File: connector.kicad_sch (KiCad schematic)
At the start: 83 parts, among them J1 USB_C_Receptacle_USB2.0_16P, J10 POWER2, J11 TELEM1, J12 TELEM2, J13 GPS, J14 SERIAL4, J15 SERIAL5, J16 I2C, J17 CAN, J18 BUZZER, J19 Conn_01x05_Pin, J2 Micro_SD_Card_Det1, J20 ADC, J21 SPI, J22 SAFETY, J23 CAN2, J24 SBUS, J3 S_TOP_SIG, J4 S_TOP_PWR, J5 S_TOP_GND, J6 S_SIDE_SIG, J7 S_SIDE_PWR, J8 S_SIDE_GND, J9 POWER1, Q1 AO3400A, U12 USBLC6-2SC6

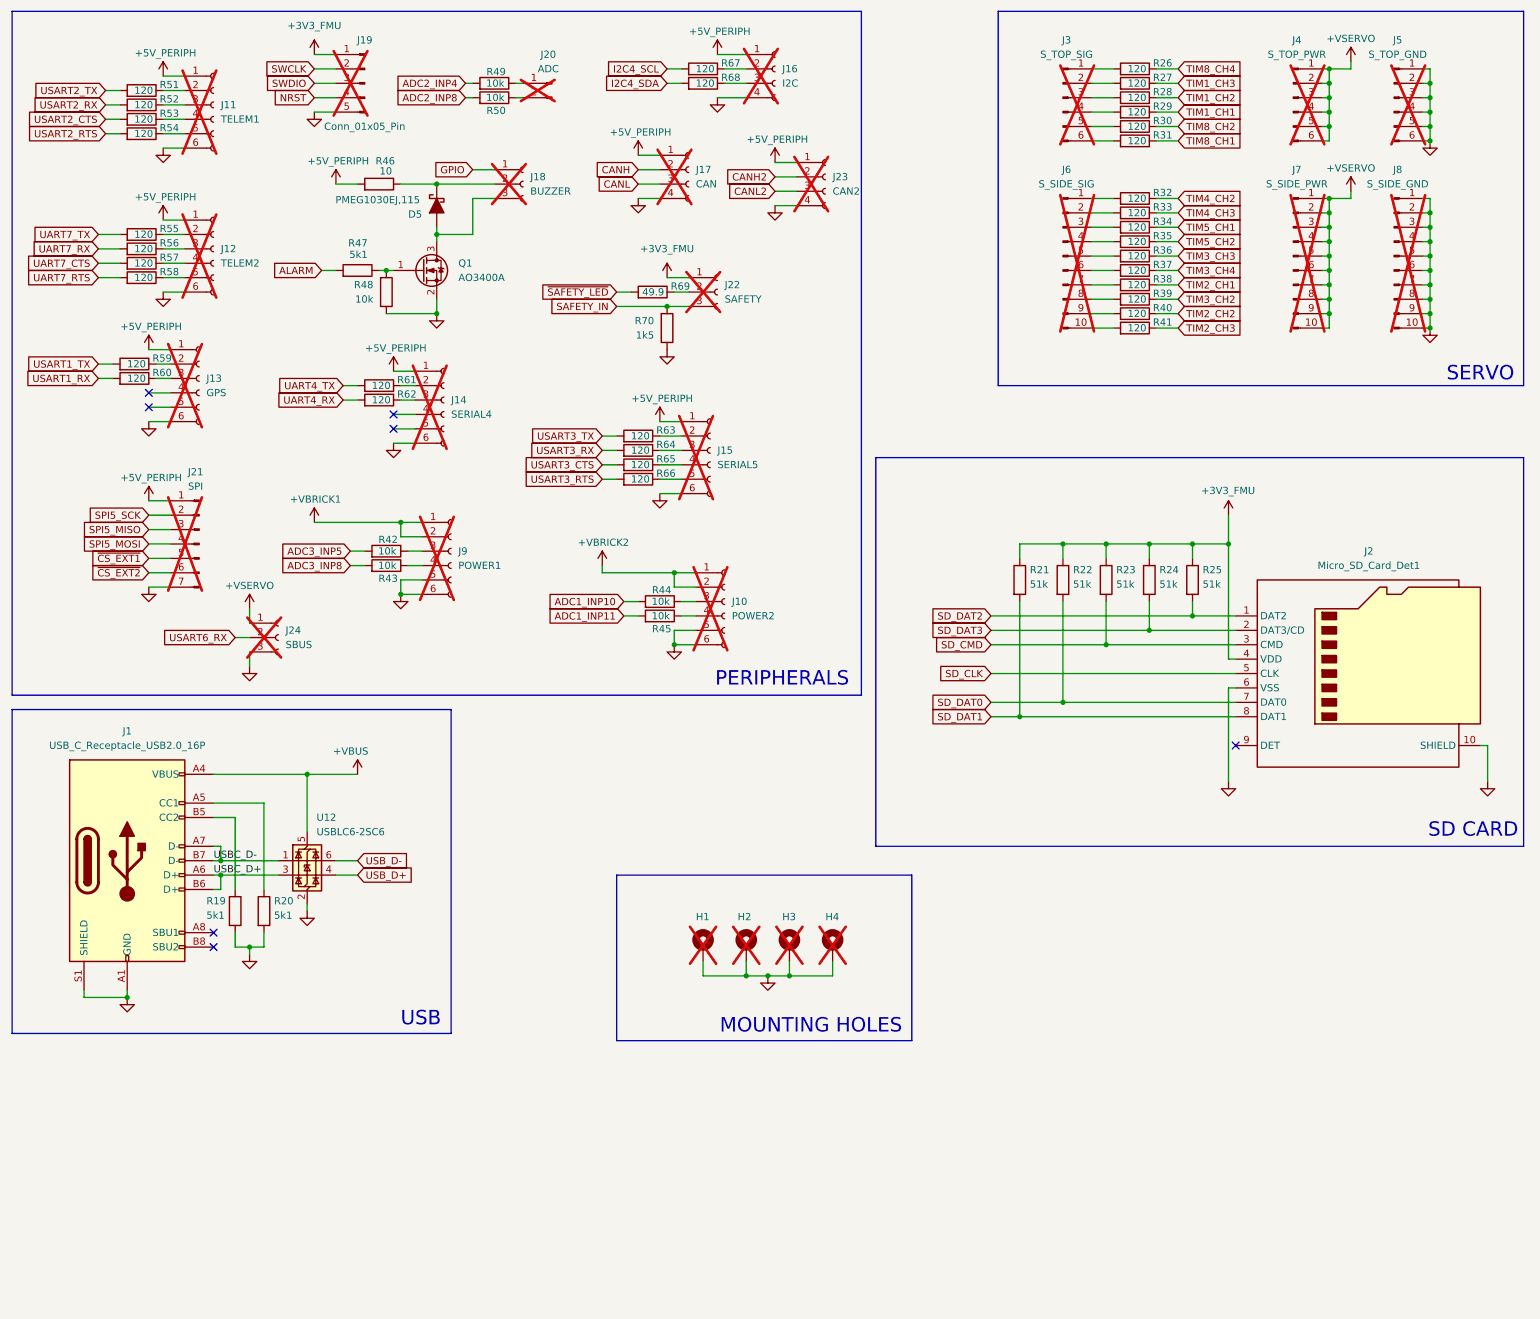
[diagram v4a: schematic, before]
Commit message: Schematic: sensor redundancy + blok current limiter GPS (terverifikasi)
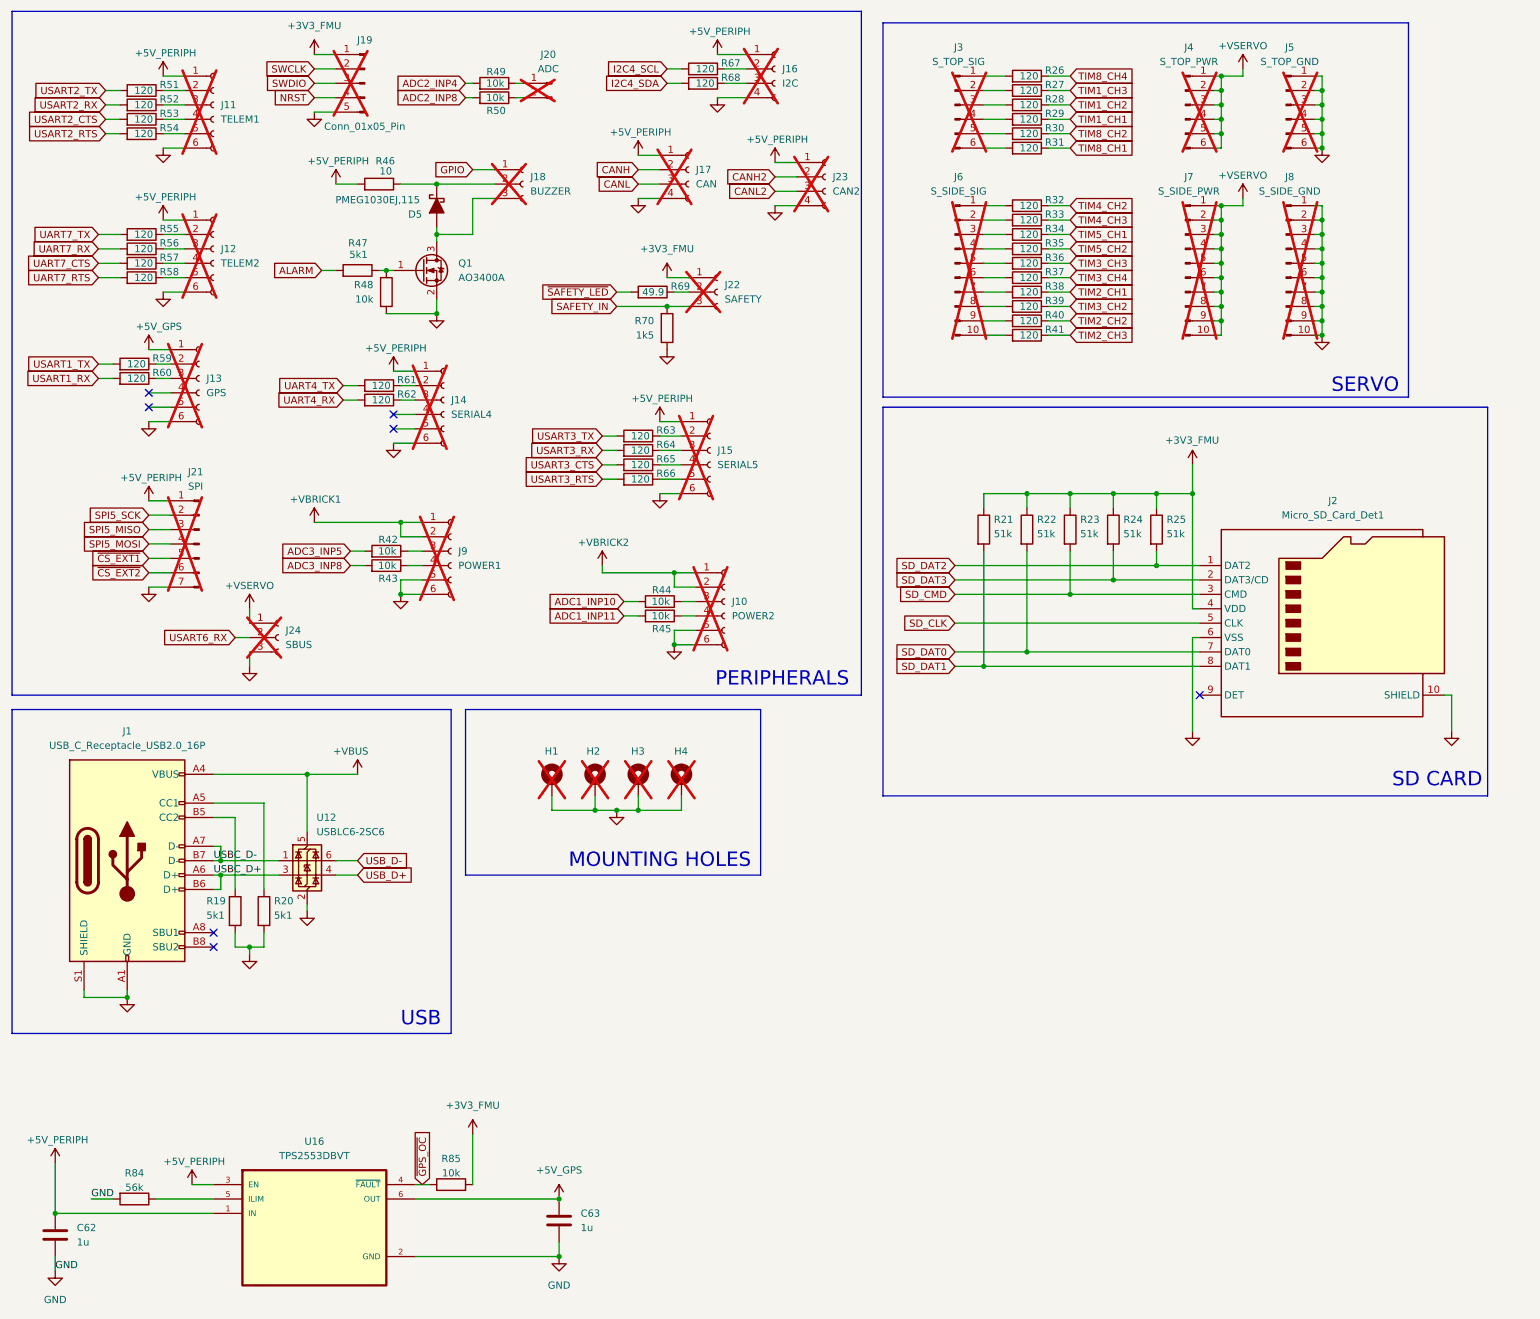
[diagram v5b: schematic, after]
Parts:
- added C62, C63: 1u, Capacitor_SMD:C_0603_1608Metric, symbol Device:C
- added R84: 56k, Resistor_SMD:R_0402_1005Metric, symbol Device:R
- added R85: 10k, Resistor_SMD:R_0402_1005Metric, symbol Device:R
- added U16: TPS2553DBVT, Svayam:SOT95P280X145-6N, symbol Svayam_Symbol:TPS2553DBVT
- J2: footprint easyeda2kicad:SIM-SMD_8P-1040310811 -> Svayam:104031-0811_MOL
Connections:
- net +3V3_FMU: now also R85.2
- net +5V_PERIPH: now also C62.1, U16.1 (IN), U16.3 (EN); no longer J13.1 (Pin_1)
- net GND: now also C62.2, C63.2, R84.2, U16.2 (GND)
- new net: R84.1, U16.5 (ILIM)
- new net +5V_GPS: C63.1, J13.1 (Pin_1), U16.6 (OUT)
- new net ~{GPS_OC}: R85.1, U16.4 (~{FAULT})
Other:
- moved on the sheet: H1, H2, H3, H4, J2, J3, J4, J5, J6, J7, J8, R21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

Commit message: Schematic: 9-port current limiter selesai (GPS..SPI, verified pass-6)
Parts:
- added C64, C65, C66, C67, C68, C69, C70, C71, C72, C73, C74, C75, C76, C77, C78, C79: 1u, Capacitor_SMD:C_0603_1608Metric, symbol Device:C
- added R100, R94: 110k, Resistor_SMD:R_0402_1005Metric, symbol Device:R
- added R101, R87, R89, R92, R93, R96, R97, R99: 10k, Resistor_SMD:R_0402_1005Metric, symbol Device:R
- added R86, R88: 33k, Resistor_SMD:R_0402_1005Metric, symbol Device:R
- added R90, R91, R95, R98: 75k, Resistor_SMD:R_0402_1005Metric, symbol Device:R
- added U17, U18, U19, U20, U21, U22, U23, U24: TPS2553DBVT, Svayam:SOT95P280X145-6N, symbol Svayam_Symbol:TPS2553DBVT
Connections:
- net +3V3_FMU: now also R101.2, R87.2, R89.2, R92.2, R93.2, R96.2, R97.2, R99.2
- net +5V_PERIPH: now also C64.1, C66.1, C68.1, C69.1, C72.1, C73.1, C76.1, C78.1, U17.1 (IN), U17.3 (EN), U18.1 (IN), U18.3 (EN), U19.1 (IN), U19.3 (EN), U20.1 (IN), U20.3 (EN), U21.1 (IN), U21.3 (EN), U22.1 (IN), U22.3 (EN), U23.1 (IN), U23.3 (EN), U24.1 (IN), U24.3 (EN); no longer J11.1 (Pin_1), J12.1 (Pin_1), J14.1 (Pin_1), J15.1 (Pin_1), J16.1 (Pin_1), J17.1 (Pin_1), J21.1 (Pin_1), J23.1 (Pin_1)
- net GND: now also C64.2, C65.2, C66.2, C67.2, C68.2, C69.2, C70.2, C71.2, C72.2, C73.2, C74.2, C75.2, C76.2, C77.2, C78.2, C79.2, R100.2, R86.2, R88.2, R90.2, R91.2, R94.2, R95.2, R98.2, U17.2 (GND), U18.2 (GND), U19.2 (GND), U20.2 (GND), U21.2 (GND), U22.2 (GND), U23.2 (GND), U24.2 (GND)
- new net: R98.1, U23.5 (ILIM)
- new net: R86.1, U17.5 (ILIM)
- new net: R91.1, U20.5 (ILIM)
- new net: R88.1, U18.5 (ILIM)
- new net: R90.1, U19.5 (ILIM)
- new net: R100.1, U24.5 (ILIM)
- new net: R95.1, U22.5 (ILIM)
- new net: R94.1, U21.5 (ILIM)
- new net +5V_CAN: C75.1, J17.1 (Pin_1), U22.6 (OUT)
- new net +5V_CAN2: C77.1, J23.1 (Pin_1), U23.6 (OUT)
- new net +5V_I2C: C74.1, J16.1 (Pin_1), U21.6 (OUT)
- new net +5V_SERIAL4: C70.1, J14.1 (Pin_1), U19.6 (OUT)
- new net +5V_SERIAL5: C71.1, J15.1 (Pin_1), U20.6 (OUT)
- new net +5V_SPI: C79.1, J21.1 (Pin_1), U24.6 (OUT)
- new net +5V_TELEM1: C67.1, J11.1 (Pin_1), U18.6 (OUT)
- new net +5V_TELEM2: C65.1, J12.1 (Pin_1), U17.6 (OUT)
- new net ~{CAN2_OC}: R99.1, U23.4 (~{FAULT})
- new net ~{CAN_OC}: R97.1, U22.4 (~{FAULT})
- new net ~{I2C_OC}: R96.1, U21.4 (~{FAULT})
- new net ~{SERIAL4_OC}: R92.1, U19.4 (~{FAULT})
- new net ~{SERIAL5_OC}: R93.1, U20.4 (~{FAULT})
- new net ~{SPI_OC}: R101.1, U24.4 (~{FAULT})
- new net ~{TELEM1_OC}: R89.1, U18.4 (~{FAULT})
- new net ~{TELEM2_OC}: R87.1, U17.4 (~{FAULT})
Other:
- moved on the sheet: C62, C63, R84, R85, U16

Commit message: Schematic: proteksi +VSERVO lengkap (TVS SMAJ6.0A + bulk + 16x1uF per-port) + konektor servo 3-pin + OC ke MCU; ERC 55 (verified)
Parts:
- removed J3: S_TOP_SIG, Connector_PinHeader_2.54mm:PinHeader_1x06_P2.54mm_Vertical, symbol Connector:Conn_01x06_Pin
- removed J4: S_TOP_PWR, Connector_PinHeader_2.54mm:PinHeader_1x06_P2.54mm_Vertical, symbol Connector:Conn_01x06_Pin
- removed J5: S_TOP_GND, Connector_PinHeader_2.54mm:PinHeader_1x06_P2.54mm_Vertical, symbol Connector:Conn_01x06_Pin
- removed J6: S_SIDE_SIG, Connector_PinHeader_2.54mm:PinHeader_1x10_P2.54mm_Vertical, symbol Connector:Conn_01x10_Pin
- removed J7: S_SIDE_PWR, Connector_PinHeader_2.54mm:PinHeader_1x10_P2.54mm_Vertical, symbol Connector:Conn_01x10_Pin
- removed J8: S_SIDE_GND, Connector_PinHeader_2.54mm:PinHeader_1x10_P2.54mm_Vertical, symbol Connector:Conn_01x10_Pin
- removed R34, R35, R36, R37, R38, R39, R40, R41: 120, Resistor_SMD:R_0402_1005Metric, symbol Device:R
- added C100, C101, C104, C105, C108, C109, C114, C115, C116, C117, C118, C119, C120, C121, C122, C123, C97: 100n, Capacitor_SMD:C_0402_1005Metric, symbol Device:C
- added C102, C103, C106, C107, C110, C111, C113, C80, C83, C85, C87, C89, C91, C93, C95, C98, C99: 1u, Capacitor_SMD:C_0603_1608Metric, symbol Device:C
- added C112: 220u, Capacitor_SMD:CP_Elec_6.3x7.7, symbol Device:C
- added D8: SMAJ6.0A, Diode_SMD:D_SMA, symbol Diode:SMAJ6.0A
- added J25: Channel 1, symbol Connector:Conn_01x03_Pin
- added J26: Channel 2, symbol Connector:Conn_01x03_Pin
- added J27: Channel 3, symbol Connector:Conn_01x03_Pin
- added J28: Channel 4, symbol Connector:Conn_01x03_Pin
- added J41: Channel 5, symbol Connector:Conn_01x03_Pin
- added J42: Channel 6, symbol Connector:Conn_01x03_Pin
- added J43: Channel 7, symbol Connector:Conn_01x03_Pin
- added J44: Channel 8, symbol Connector:Conn_01x03_Pin
- added J45: Channel 13, symbol Connector:Conn_01x03_Pin
- added J46: Channel 9, symbol Connector:Conn_01x03_Pin
- added J47: Channel 14, symbol Connector:Conn_01x03_Pin
- added J48: Channel 10, symbol Connector:Conn_01x03_Pin
- added J49: Channel 15, symbol Connector:Conn_01x03_Pin
- added J50: Channel 11, symbol Connector:Conn_01x03_Pin
- added J51: Channel 16, symbol Connector:Conn_01x03_Pin
- added J52: Channel 12, symbol Connector:Conn_01x03_Pin
- added R102, R103, R116, R117, R118, R119, R120, R121: 120, Resistor_SMD:R_0402_1005Metric, symbol Device:R
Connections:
- net +VSERVO: now also C102.1, C103.1, C106.1, C107.1, C110.1, C111.1, C112.1, C113.1, C114.1, C80.1, C83.1, C85.1, C87.1, C89.1, C91.1, C93.1, C95.1, C98.1, C99.1, D8.1 (A1), J25.1 (Pin_1), J26.1 (Pin_1), J27.1 (Pin_1), J28.1 (Pin_1), J41.1 (Pin_1), J42.1 (Pin_1), J43.1 (Pin_1), J44.1 (Pin_1), J45.1 (Pin_1), J46.1 (Pin_1), J47.1 (Pin_1), J48.1 (Pin_1), J49.1 (Pin_1), J50.1 (Pin_1), J51.1 (Pin_1), J52.1 (Pin_1)
- net GND: now also C100.2, C101.2, C102.2, C103.2, C104.2, C105.2, C106.2, C107.2, C108.2, C109.2, C110.2, C111.2, C112.2, C113.2, C114.2, C115.2, C116.2, C117.2, C118.2, C119.2, C120.2, C121.2, C122.2, C123.2, C80.2, C83.2, C85.2, C87.2, C89.2, C91.2, C93.2, C95.2, C97.2, C98.2, C99.2, D8.2 (A2), J25.2 (Pin_2), J26.2 (Pin_2), J27.2 (Pin_2), J28.2 (Pin_2), J41.2 (Pin_2), J42.2 (Pin_2), J43.2 (Pin_2), J44.2 (Pin_2), J45.2 (Pin_2), J46.2 (Pin_2), J47.2 (Pin_2), J48.2 (Pin_2), J49.2 (Pin_2), J50.2 (Pin_2), J51.2 (Pin_2), J52.2 (Pin_2)
- net TIM1_CH1: now also R103.1; no longer R29.1
- net TIM1_CH2: now also R102.1; no longer R28.1
- net TIM2_CH1: now also R30.1
- net TIM2_CH2: now also R118.1
- net TIM2_CH3: now also R120.1
- net TIM3_CH2: now also R32.1
- net TIM3_CH3: now also R119.1
- net TIM3_CH4: now also R121.1
- net TIM4_CH2: now also R116.1; no longer R32.1
- net TIM4_CH3: now also R117.1; no longer R33.1
- net TIM5_CH1: now also R31.1
- net TIM5_CH2: now also R33.1
- net TIM8_CH1: now also R29.1; no longer R31.1
- net TIM8_CH2: now also R28.1; no longer R30.1
- net at R27.2: now also C121.1, J26.3 (Pin_3)
- net at R32.2: now also C100.1, J47.3 (Pin_3)
- net at R29.2: now also C117.1, J42.3 (Pin_3)
- net at R28.2: now also C116.1, J41.3 (Pin_3)
- net at R33.2: now also C108.1, J48.3 (Pin_3)
- net at R31.2: now also C105.1, J46.3 (Pin_3)
- net at R26.2: now also C120.1, J25.3 (Pin_3)
- net at R30.2: now also C97.1, J45.3 (Pin_3)
- new net: C123.1, J28.3 (Pin_3), R103.2
- new net: C101.1, J49.3 (Pin_3), R118.2
- new net: C104.1, J51.3 (Pin_3), R120.2
- new net: C115.1, J52.3 (Pin_3), R121.2
- new net: C109.1, J50.3 (Pin_3), R119.2
- new net: C119.1, J44.3 (Pin_3), R117.2
- new net: C122.1, J27.3 (Pin_3), R102.2
- new net: C118.1, J43.3 (Pin_3), R116.2
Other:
- note removed: "SERVO"
- moved on the sheet: C62, C63, C64, C65, C66, C67, C68, C69, C70, C71, C72, C73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

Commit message: Connector: RILIM CAN/CAN2 75k->47k (passive CAN splitter); RCIN J24->USART6_RX verified (0E/17W)
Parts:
- R95, R98: value 75k -> 47k
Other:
- note added: "IMAX = 616mA"
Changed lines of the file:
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@@
 		)
 	)
+	(text "IMAX = 616mA\n"
+		(exclude_from_sim no)
+		(at 501.65 231.14 0)
+		(effects
+			(font
+				(size 1.27 1.27)
+			)
+		)
+	)
 	(text "PERIPHERALS\n"
 		(exclude_from_sim no)
@@
 		)
 	)
+	(text "IMAX = 616mA\n"
+		(exclude_from_sim no)
+		(at 501.396 305.562 0)
+		(effects
+			(font
+				(size 1.27 1.27)
+			)
+		)
+	)
 	(text "USB\n"
 		(exclude_from_sim no)
@@
 			)
 		)
-		(property "Value" "75k"
+		(property "Value" "47k"
 			(at 492.76 222.758 90)
 			(show_name no)
@@
 			)
 		)
-		(property "Value" "75k"
+		(property "Value" "47k"
 			(at 494.03 296.418 90)
 			(show_name no)
